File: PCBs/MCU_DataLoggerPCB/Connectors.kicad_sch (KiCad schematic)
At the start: 4 parts, among them J1 Conn_01x04_Pin, J2 Conn_01x04_Pin, J3 Conn_01x09_Pin, J4 Conn_02x03_Odd_Even

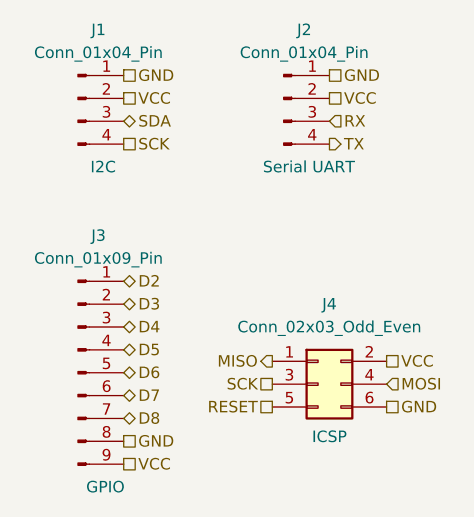
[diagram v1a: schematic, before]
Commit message: Project: Fix defect with SCK and SCL clocks in the schematic
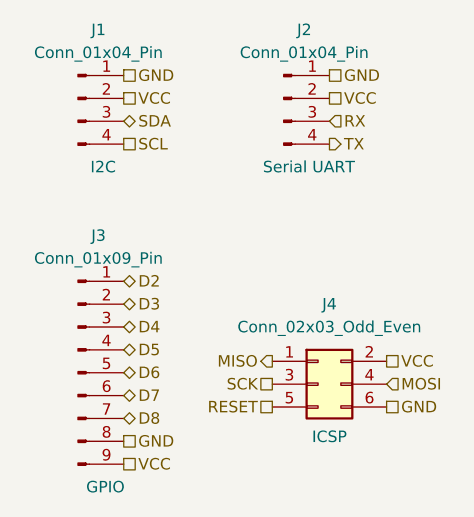
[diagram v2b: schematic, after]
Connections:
- net SCK: no longer J1.4 (Pin_4)
- new net SCL: J1.4 (Pin_4)
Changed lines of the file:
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@@
 		)
 	)
-	(hierarchical_label "SCK"
+	(hierarchical_label "SCL"
 		(shape passive)
 		(at 142.24 99.06 0)
